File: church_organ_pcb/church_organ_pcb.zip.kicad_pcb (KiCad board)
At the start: 2 copper layers, 69.9 x 120.5 mm, 51 parts, among them J1 4.5-28V Power Input, J2 USB, J3 Fan 1, J4 Fan 2, U1 AP63205WU, U2 WT32-ETH01, U3 WT32-ETH01, U4 SN74HC125DR, U5 CH340C, U6 AMS1117-3.3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

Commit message: removed fan outputs and regulator, fixed traces and removed esp32s, made holes bigger for screws
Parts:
- removed C8: 10uF, Capacitor_SMD:C_0805_2012Metric_Pad1.18x1.45mm_HandSolder
- removed C9: 22uF, Capacitor_SMD:C_0805_2012Metric_Pad1.18x1.45mm_HandSolder
- removed G***: LOGO, LOGO
- removed J3: Fan 1, Connector_JST:JST_XH_B2B-XH-A_1x02_P2.50mm_Vertical
- removed J4: Fan 2, Connector_JST:JST_XH_B2B-XH-A_1x02_P2.50mm_Vertical
- removed U2, U3: WT32-ETH01, WT32-ETH01:WT32_ETH01
- removed U6: AMS1117-3.3, Package_TO_SOT_SMD:SOT-223-3_TabPin2
- added J5: Conn_01x13_Socket, Connector_PinSocket_2.54mm:PinSocket_1x13_P2.54mm_Vertical, F.Cu at (119.1, 77.4)
- added J6: Conn_01x13_Socket, Connector_PinSocket_2.54mm:PinSocket_1x13_P2.54mm_Vertical, F.Cu at (141.9, 77.4)
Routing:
- net 3V3: track 85.5 -> 48.4 mm
- net Port-4: track 60.4 -> 24.3 mm
- net Port-2: track 49.2 -> 17.9 mm
- net IO0: track 100.0 -> 68.8 mm
- net F5V: track 28.8 -> 0.00 mm
- net Port-3: track 51.1 -> 22.4 mm
- net VOUT: track 120.8 -> 93.9 mm
- net GND: track 441.3 -> 467.8 mm
- net Port-1: track 47.7 -> 21.2 mm
- net RPP: track 324.1 -> 298.8 mm
- net Port-7: track 38.3 -> 14.7 mm
- net Port-5: track 42.0 -> 21.3 mm, vias 1 -> 0
- net Port-8: track 37.3 -> 26.4 mm, vias 1 -> 0
- net Port-6: track 34.9 -> 25.6 mm, vias 0 -> 2
- net EN: track 72.1 -> 66.6 mm, vias 1 -> 2
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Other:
- outline, holes or cut-outs redrawn
- board text removed: ">"
- board text removed: "ANTENNA"
- board text removed: "Creative xLights"
- board text removed: "|"

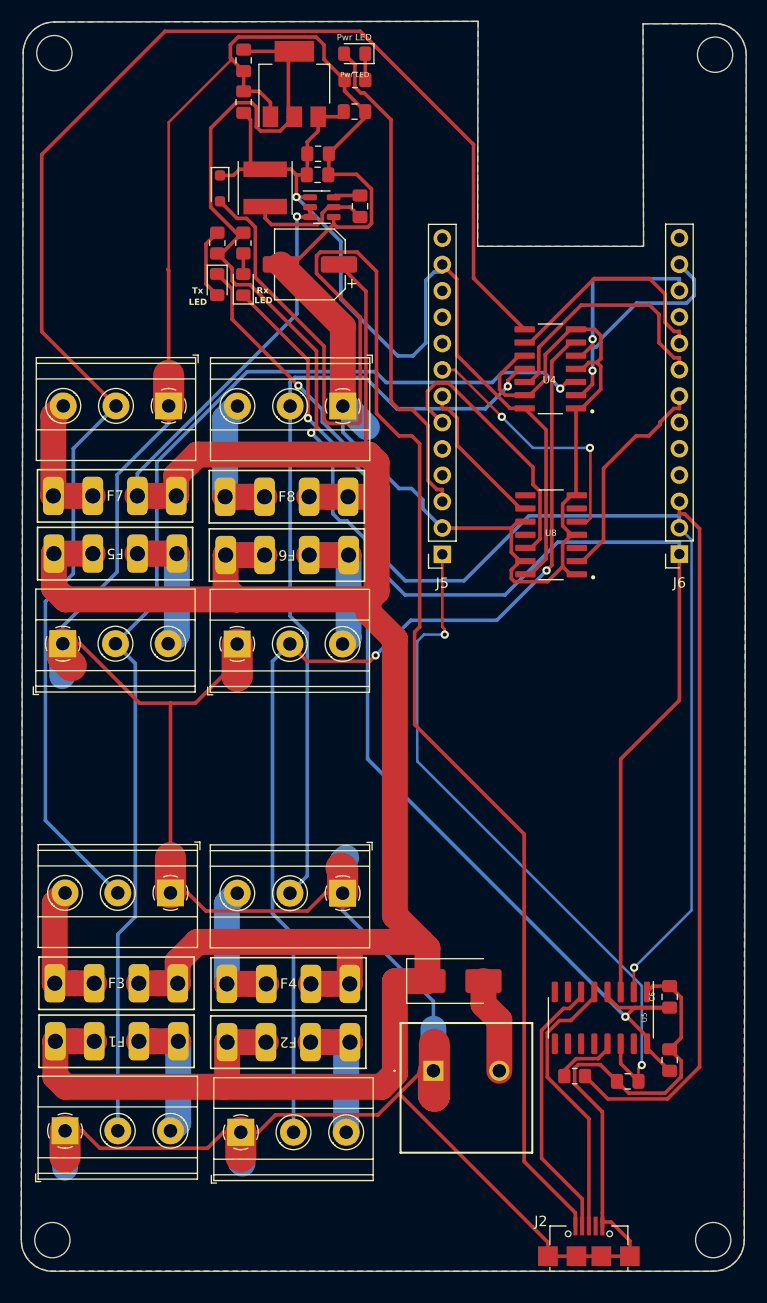
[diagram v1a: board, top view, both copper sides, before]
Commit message: Commit changes to PCB
Rerouted power traces to/from the fuses
Replaced screw terminal with quick connect terminals
Fixed an issue where LED-outputs 5,6,7,8 was not correctly connected to their NETs
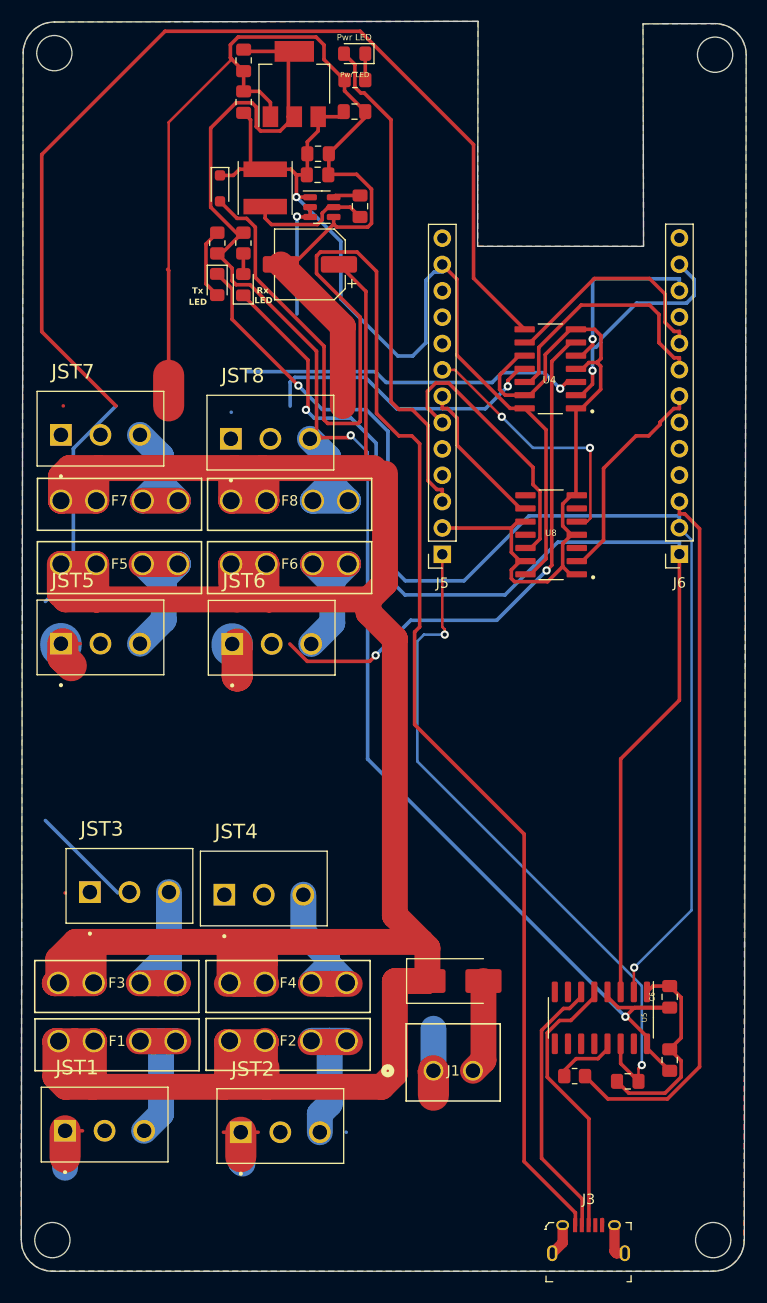
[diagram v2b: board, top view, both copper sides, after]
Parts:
- removed J2: USB, MicroUSB:USB_Micro-B_Unknown_5s_SMT
- added J3: 10118194-0001LF, digikey-footprints:USB_Micro_B_Female_10118194-0001LF, F.Cu at (133.2, 142.1)
- F1, F2, F3, F4, F5, F6, F7, F8: footprint WT32-ETH-Fuse-Holder:MCCQ-122_MTC -> 3544-fuse:CONN_3544-2_KEY
- J1: footprint SamacSys_Parts:1714955 -> terminal_block_footprints:CONN_691321300002_WRE
- JST1, JST2, JST3, JST4, JST5, JST6, JST7, JST8: footprint TerminalBlock_Phoenix:TerminalBlock_Phoenix_MKDS-1,5-3-5.08_1x03_P5.08mm_Horizontal -> 3pin:CUI_TBP02R2-381-03BE
- moved F2 11.5 mm to (98.6, 124.3), turned to 0 degrees
- moved F1 11.4 mm to (82.1, 124.3), turned to 0 degrees
- moved JST4 11.4 mm to (98.1, 110.2), turned to 0 degrees
- moved F6 11.3 mm to (98.7, 78.3), turned to 0 degrees
- moved JST8 11.2 mm to (98.7, 66.2), turned to 0 degrees
- moved F5 11.1 mm to (82.3, 78.3), turned to 0 degrees
- moved JST7 10.8 mm to (82.3, 65.9), turned to 0 degrees
- moved JST3 7.77 mm to (85.1, 109.9), turned to 0 degrees
- moved F7 0.79 mm to (82.3, 72.2)
- moved F8 0.62 mm to (98.7, 72.2)
- moved JST6 0.48 mm to (98.8, 86.0)
- moved F3 0.24 mm to (82.1, 118.7)
- moved F4 0.19 mm to (98.6, 118.7)
- moved JST5 0.18 mm to (82.3, 86.0)
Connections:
- F1 pad 1: Net-(JST1-Pin_3) -> RPP
- F1 pad 2: Net-(JST1-Pin_3) -> RPP
- F1 pad 3: RPP -> Net-(F1-Pad3)
- F1 pad 4: RPP -> Net-(F1-Pad3)
- F2 pad 1: Net-(JST2-Pin_3) -> RPP
- F2 pad 2: Net-(JST2-Pin_3) -> RPP
- F2 pad 3: RPP -> Net-(F2-Pad3)
- F2 pad 4: RPP -> Net-(F2-Pad3)
- F3 pad 1: Net-(JST3-Pin_3) -> RPP
- F3 pad 2: Net-(JST3-Pin_3) -> RPP
- F3 pad 3: RPP -> Net-(F3-Pad3)
- F3 pad 4: RPP -> Net-(F3-Pad3)
- F4 pad 1: Net-(JST4-Pin_3) -> RPP
- F4 pad 2: Net-(JST4-Pin_3) -> RPP
- F4 pad 3: RPP -> Net-(F4-Pad3)
- F4 pad 4: RPP -> Net-(F4-Pad3)
- F5 pad 1: Net-(JST5-Pin_3) -> RPP
- F5 pad 2: Net-(JST5-Pin_3) -> RPP
- F5 pad 3: RPP -> Net-(F5-Pad3)
- F5 pad 4: RPP -> Net-(F5-Pad3)
- F6 pad 1: Net-(JST6-Pin_3) -> RPP
- F6 pad 2: Net-(JST6-Pin_3) -> RPP
- F6 pad 3: RPP -> Net-(F6-Pad3)
- F6 pad 4: RPP -> Net-(F6-Pad3)
- F7 pad 1: Net-(JST7-Pin_3) -> RPP
- F7 pad 2: Net-(JST7-Pin_3) -> RPP
- F7 pad 3: RPP -> Net-(F7-Pad3)
- F7 pad 4: RPP -> Net-(F7-Pad3)
- F8 pad 1: Net-(JST8-Pin_3) -> RPP
- F8 pad 2: Net-(JST8-Pin_3) -> RPP
- F8 pad 3: RPP -> Net-(F8-Pad3)
- F8 pad 4: RPP -> Net-(F8-Pad3)
- JST1 pad 3: Net-(JST1-Pin_3) -> Net-(F1-Pad3)
- JST2 pad 3: Net-(JST2-Pin_3) -> Net-(F2-Pad3)
- JST3 pad 3: Net-(JST3-Pin_3) -> Net-(F3-Pad3)
- JST4 pad 3: Net-(JST4-Pin_3) -> Net-(F4-Pad3)
- JST5 pad 2: Output-1 -> Output-5
- JST5 pad 3: Net-(JST5-Pin_3) -> Net-(F5-Pad3)
- JST6 pad 2: Output-2 -> Output-6
- JST6 pad 3: Net-(JST6-Pin_3) -> Net-(F6-Pad3)
- JST7 pad 2: Output-3 -> Output-7
- JST7 pad 3: Net-(JST7-Pin_3) -> Net-(F7-Pad3)
- JST8 pad 2: Output-4 -> Output-8
- JST8 pad 3: Net-(JST8-Pin_3) -> Net-(F8-Pad3)
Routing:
- net GND: track 467.8 -> 239.2 mm
- net Output-1: track 113.4 -> 33.4 mm
- net RPP: track 298.8 -> 353.3 mm
- net Output-2: track 101.1 -> 52.5 mm
- net Output-4: track 76.6 -> 28.3 mm
- net Net-(F5-Pad3): track 0.00 -> 21.3 mm
- net Output-3: track 150.8 -> 129.7 mm
- net Net-(F1-Pad3): track 0.00 -> 19.1 mm
- net Net-(F4-Pad3): track 0.00 -> 19.0 mm
- net Net-(F2-Pad3): track 0.00 -> 18.8 mm
- net Net-(F3-Pad3): track 0.00 -> 18.6 mm
- net Net-(JST8-Pin_3): track 16.2 -> 0.00 mm
- net Net-(JST4-Pin_3): track 15.3 -> 0.00 mm
- net Net-(F6-Pad3): track 0.00 -> 15.2 mm
- net Net-(JST5-Pin_3): track 15.2 -> 0.00 mm
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
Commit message: rerouted most of board
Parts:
- moved D2 53.3 mm to (122.3, 81.1)
- moved R1 53.3 mm to (122.4, 83.6)
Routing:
- net GND: track 239.2 -> 100.8 mm, vias 0 -> 2
- net Output-1: track 33.4 -> 113.6 mm, vias 1 -> 4
- net 3.3V: track 149.5 -> 229.1 mm, vias 2 -> 4
- net Output-5: track 0.00 -> 58.5 mm, vias 0 -> 1
- net Output-7: track 0.00 -> 47.8 mm, vias 0 -> 2
- net Output-2: track 52.5 -> 94.1 mm, vias 2 -> 3
- net Output-6: track 0.00 -> 39.7 mm, vias 0 -> 1
- net 3V3: track 48.4 -> 9.75 mm
- net Output-3: track 129.7 -> 91.6 mm, vias 0 -> 1
- net Output-4: track 28.3 -> 64.3 mm, vias 1 -> 4
- net Output-8: track 0.00 -> 29.8 mm, vias 0 -> 1
- net VOUT: track 93.9 -> 79.4 mm
- net Net-(U5-UD+): track 26.8 -> 31.8 mm
- net Port-2: track 17.9 -> 12.9 mm
- net RPP: track 353.3 -> 349.3 mm, vias 1 -> 2
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
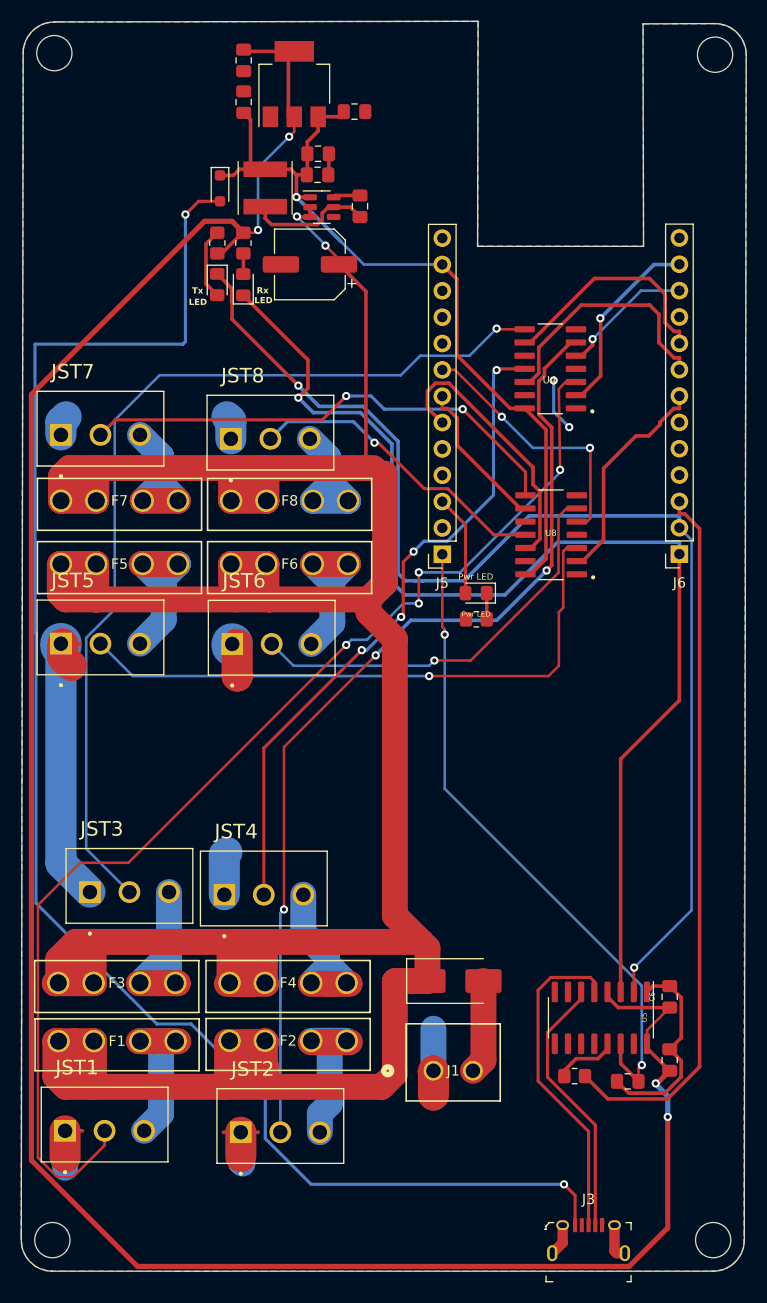
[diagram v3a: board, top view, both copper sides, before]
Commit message: Fixed scattered groundplane
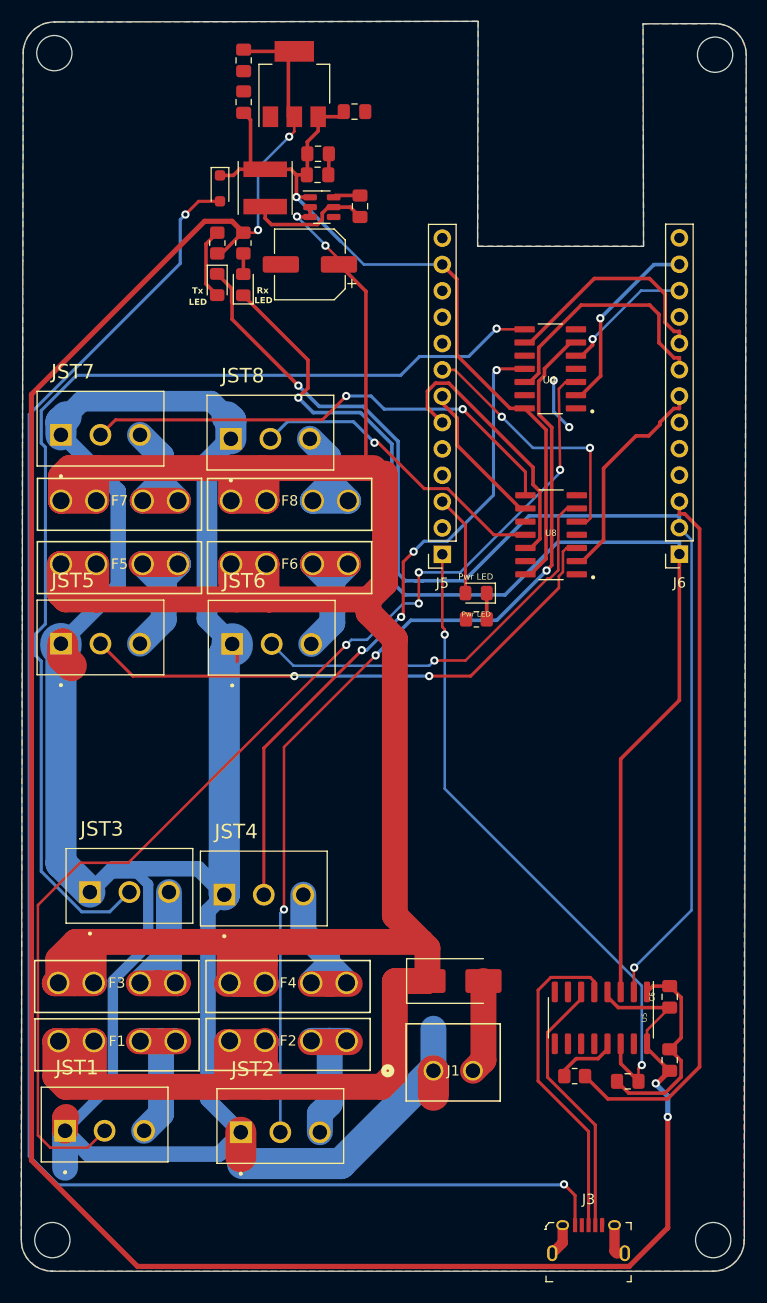
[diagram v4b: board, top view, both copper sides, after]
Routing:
- net GND: track 100.8 -> 292.1 mm
- net Output-3: track 91.6 -> 106.1 mm
- net Net-(D5-A): track 153.4 -> 158.0 mm
- net Output-1: track 113.6 -> 109.2 mm
- net Output-5: track 58.5 -> 54.2 mm, vias 1 -> 2

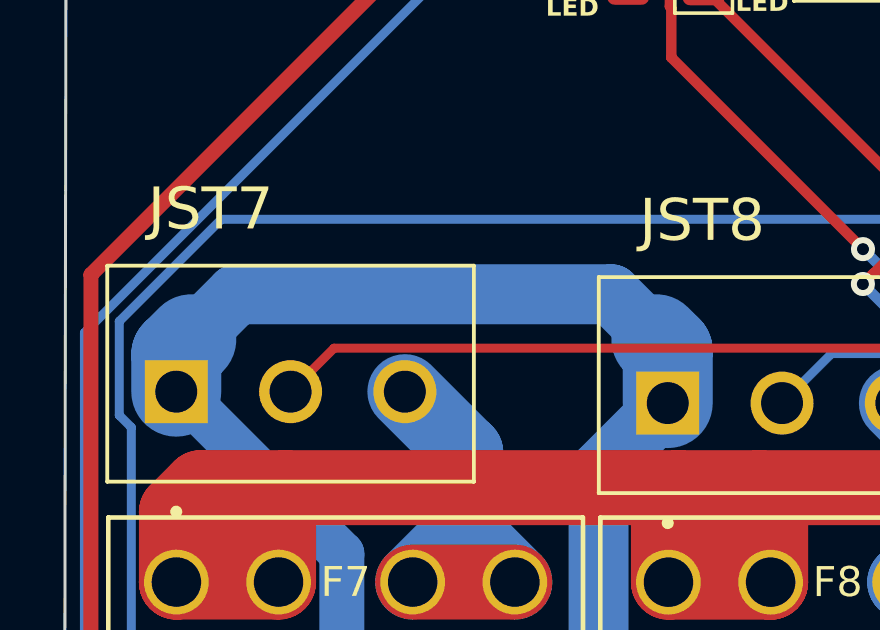
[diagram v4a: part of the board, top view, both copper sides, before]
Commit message: Added inductor to komponenter folder
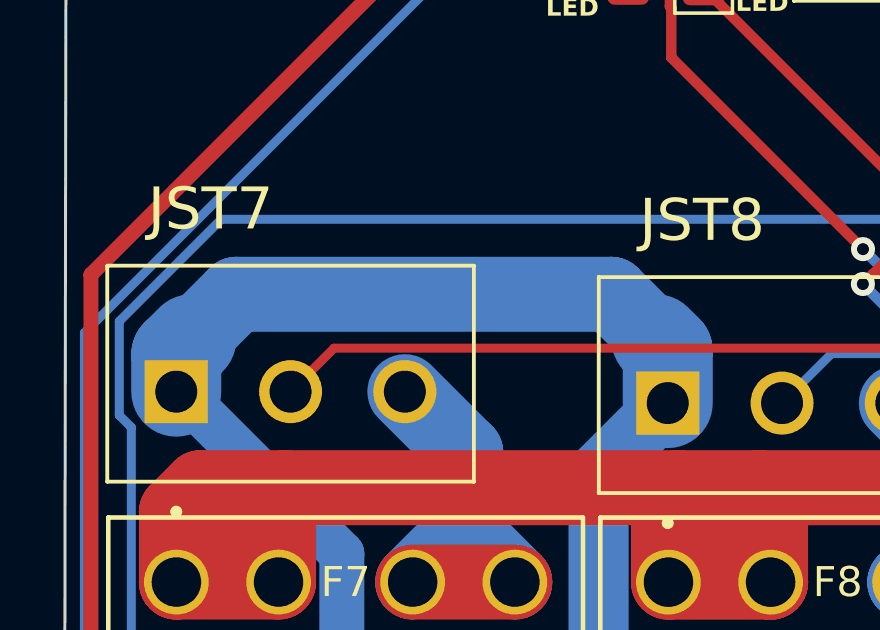
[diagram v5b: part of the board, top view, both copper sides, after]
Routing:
- net GND: track 292.1 -> 290.8 mm
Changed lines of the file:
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@@
 		(start 96.816769 62.612)
 		(end 97.812769 63.608)
-		(width 2)
+		(width 2.5)
 		(layer "B.Cu")
 		(net 2)
@@
 		(start 84.316769 62.612)
 		(end 96.816769 62.612)
-		(width 2)
+		(width 2.5)
 		(layer "B.Cu")
 		(net 2)
@@
 	)
 	(segment
-		(start 97.812769 63.608)
-		(end 98.697769 64.493)
-		(width 1.5)
-		(layer "B.Cu")
-		(net 2)
-	)
-	(segment
 		(start 129.816769 63.612)
 		(end 131.316769 65.112)
@@
 		(start 83.320769 63.608)
 		(end 84.316769 62.612)
-		(width 2)
-		(layer "B.Cu")
-		(net 2)
+		(width 2.5)
+		(layer "B.Cu")
+		(net 2)

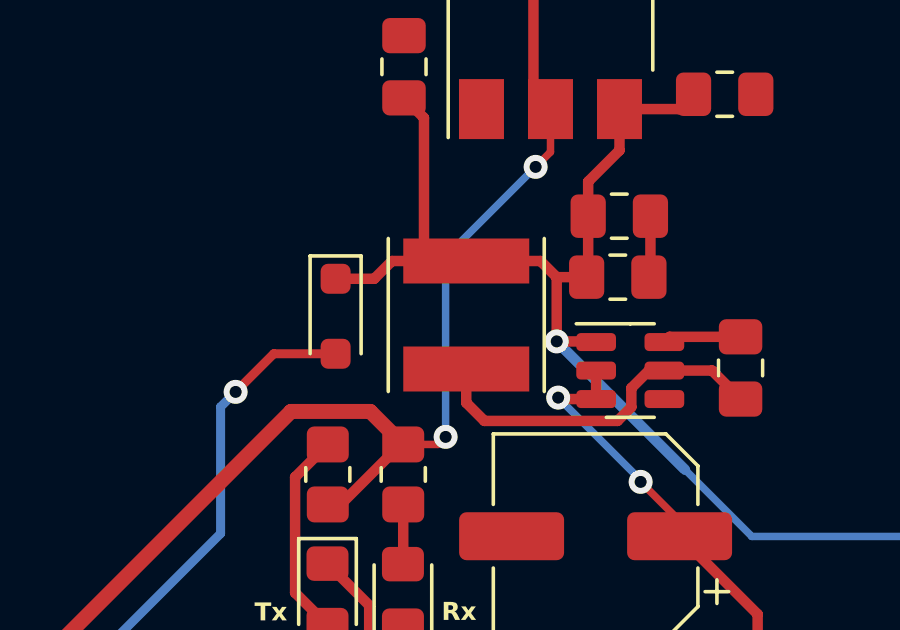
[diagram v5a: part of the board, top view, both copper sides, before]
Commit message: Add new 4.7mH inductor to voltage regulator circuit + fix 3d models
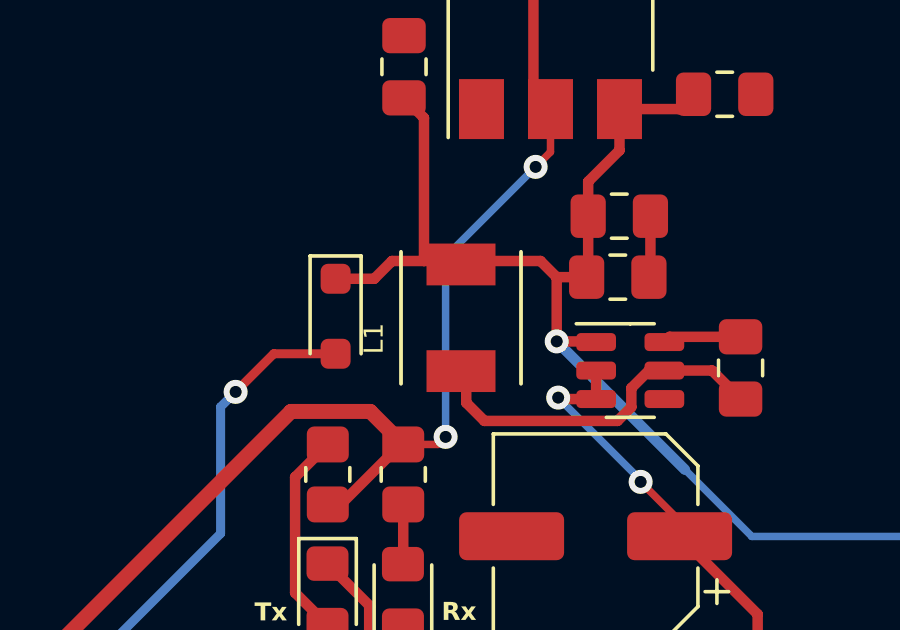
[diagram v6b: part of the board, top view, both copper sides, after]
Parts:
- JST1, JST2, JST3, JST4, JST5, JST6, JST7, JST8: footprint 3pin:CUI_TBP02R2-381-03BE -> 3pin:CUI_TBP02R2-381-03BE_+3D
- L1: value 4.7uH -> AMDLA4020S-4R7MT; footprint Inductor_SMD:L_Taiyo-Yuden_MD-5050 -> AMDLA4020S-4R7MT:IND_AMDLA4020S-4R7MT
- moved L1 0.20 mm to (101.8, 42.1)
